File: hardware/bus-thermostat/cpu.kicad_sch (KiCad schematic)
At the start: 28 parts, among them J1 Conn_01x03_Female, J2 RJ45_Shielded, U7 ATtiny424-X, U8 PCA9615DP, U9 MC33660BEFR2

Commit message: Redid the 24VAC path entirely.
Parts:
- renumbered C13 to C21, C14 to C22, C15 to C23, C16 to C24, D11 to D10, D6 to D5, D7 to D6, D8 to D7, D9 to D8, D10 to D9, R20 to R21, R21 to R22, R22 to R23, R23 to R24, R24 to R25, R25 to R26, R26 to R27, R27 to R28, R28 to R29, R29 to R30, R30 to R31, R31 to R32, R32 to R33

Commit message: First rev of thermostat firmware
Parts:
- removed J1: Conn_01x03_Female, symbol Connector:Conn_01x03_Female
- added D?: BAT42W-V, Diode_SMD:D_SOD-123, symbol Diode:BAT42W-V
- added J?: FTDI Serial, SparkFun-Connectors:6_PIN_SERIAL_TARGET_SIDE_W_SILK, symbol SparkFun-Connectors:6_PIN_SERIAL_TARGETSILK
- added JP?: Solder Jumper, Jumper:SolderJumper-2_P1.3mm_Open_TrianglePad1.0x1.5mm, symbol Jumper:SolderJumper_2_Open
- added R?: 470R, symbol Device:R
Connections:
- net +3V3: now also JP?.2 (B)
- net GND: now also J?.GND (6)
- net I2C_EN: no longer U7.7 (PB2)
- net K_LINE_RX: now also U7.6 (PB3); no longer U7.12 (PA2)
- net K_LINE_TX: now also R29.2, U7.7 (PB2); no longer U7.11 (PA1)
- net UPDI: now also D?.2 (A), J?.RXI (2)
- net ~{RESET}: now also U7.12 (PA2); no longer R29.2, U7.6 (PB3)
- new net: D?.1 (K), R?.1
- new net: J?.TXO (3), R?.2
- new net: J?.VCC (4), JP?.1 (A)
- new net OSC_PRIME: U7.11 (PA1)
- no-connect marks 4 -> 6

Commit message: Rework the AC path generation again. Opamps only.
- awaiting the completion of analog circuit analysis
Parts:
- gave numbers to parts that had none: 4
- renumbered D8 to D10, D9 to D11, D10 to D12, D5 to D6, D6 to D7, D7 to D8, J2 to J4, R21 to R23, R22 to R24, R23 to R25, R24 to R26, R25 to R27, R26 to R28, R27 to R29, R28 to R30, R29 to R31, R30 to R32, R31 to R33, R32 to R34, R33 to R36, U9 to U10, U7 to U8, U8 to U9

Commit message: Update some components
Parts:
- removed D10: D, symbol Device:D
- added D10: ACDBQC0130L-HF, Diode_SMD:D_SOD-923, symbol Device:D_Schottky
- D11: value 45V Zener -> MMSZ5260C-E3-08; footprint (none) -> Diode_SMD:D_SOD-123
- D12: value 27V Zener -> BZT52C27-7-F; footprint (none) -> Diode_SMD:D_SOD-123
- D6, D7, D8: footprint (none) -> LED_SMD:LED_0805_2012Metric_Pad1.15x1.40mm_HandSolder
- J4: footprint (none) -> SparkFun-Connectors:RJ45-8
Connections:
- net +12V: now also D10.2 (A)
- net at R36.1: now also D10.1 (K)
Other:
- note added: "27V Zener 500mw"
- note added: "43V Zener 500mW"

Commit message: Fix oscillator, add fan controller/thermostat and its IOs.
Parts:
- added R37: 10k, Resistor_SMD:R_0805_2012Metric_Pad1.20x1.40mm_HandSolder, symbol Device:R
- C23: renamed from C21; footprint (none) -> Capacitor_SMD:C_0805_2012Metric_Pad1.18x1.45mm_HandSolder
- C24: renamed from C22; footprint (none) -> Capacitor_SMD:C_0805_2012Metric_Pad1.18x1.45mm_HandSolder
- C25: renamed from C23; footprint (none) -> Capacitor_SMD:C_0805_2012Metric_Pad1.18x1.45mm_HandSolder
- C26: renamed from C24; footprint (none) -> Capacitor_SMD:C_0805_2012Metric_Pad1.18x1.45mm_HandSolder
- J3: footprint SparkFun-Connectors:6_PIN_SERIAL_TARGET_SIDE_W_SILK -> Beirdo:FTDI_BASIC
- R28: renamed from R23; footprint (none) -> Resistor_SMD:R_0805_2012Metric_Pad1.20x1.40mm_HandSolder
- R29: renamed from R24; footprint (none) -> Resistor_SMD:R_0805_2012Metric_Pad1.20x1.40mm_HandSolder
- R30: renamed from R25; footprint (none) -> Resistor_SMD:R_0805_2012Metric_Pad1.20x1.40mm_HandSolder
- R31: renamed from R26; footprint (none) -> Resistor_SMD:R_0805_2012Metric_Pad1.20x1.40mm_HandSolder
- R32: renamed from R27; footprint (none) -> Resistor_SMD:R_0805_2012Metric_Pad1.20x1.40mm_HandSolder
- R33: renamed from R28; footprint (none) -> Resistor_SMD:R_0805_2012Metric_Pad1.20x1.40mm_HandSolder
- R34: renamed from R29; footprint (none) -> Resistor_SMD:R_0805_2012Metric_Pad1.20x1.40mm_HandSolder
- R35: renamed from R30; footprint (none) -> Resistor_SMD:R_0805_2012Metric_Pad1.20x1.40mm_HandSolder
- R36: renamed from R31; footprint (none) -> Resistor_SMD:R_0805_2012Metric_Pad1.20x1.40mm_HandSolder
- R38: renamed from R32; footprint (none) -> Resistor_SMD:R_0805_2012Metric_Pad1.20x1.40mm_HandSolder
- R39: renamed from R33; footprint (none) -> Resistor_SMD:R_0805_2012Metric_Pad1.20x1.40mm_HandSolder
- R40: renamed from R34; footprint (none) -> Resistor_SMD:R_0805_2012Metric_Pad1.20x1.40mm_HandSolder
- R41: renamed from R35; footprint (none) -> Resistor_SMD:R_0805_2012Metric_Pad1.20x1.40mm_HandSolder
- R42: renamed from R36; footprint (none) -> Resistor_SMD:R_0805_2012Metric_Pad1.20x1.40mm_HandSolder
- renumbered U9 to U10, U10 to U11, U8 to U9
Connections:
- net OSC_PRIME is gone; now on net K_LINE_EN: U9.11 (PA1)
- net +3V3: now also R37.1
- net K_LINE_EN: no longer U9.13 (PA3)
- net ~{K_LINE_LED}: now also U9.13 (PA3); no longer U9.4 (PA6)
- new net ~{FAN_FAULT}: R37.2, U9.4 (PA6)
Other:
- moved on the sheet: C23

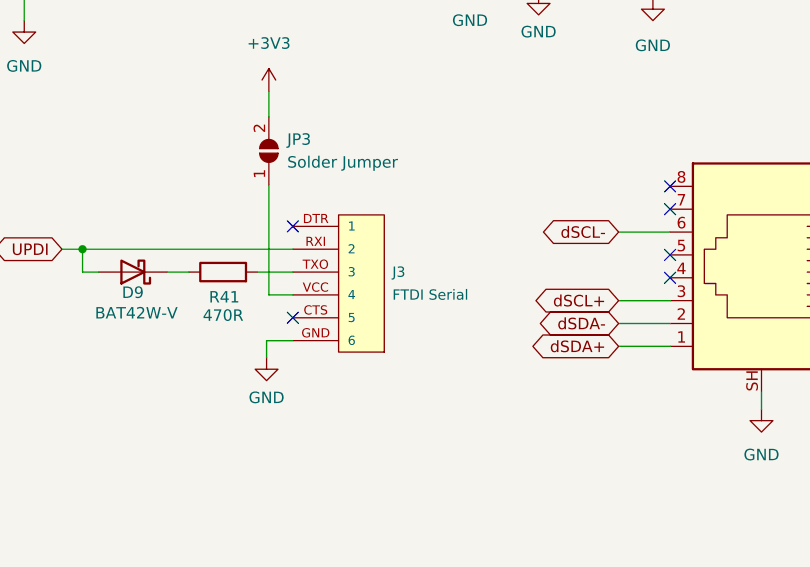
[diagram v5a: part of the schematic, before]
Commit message: Added serial ports
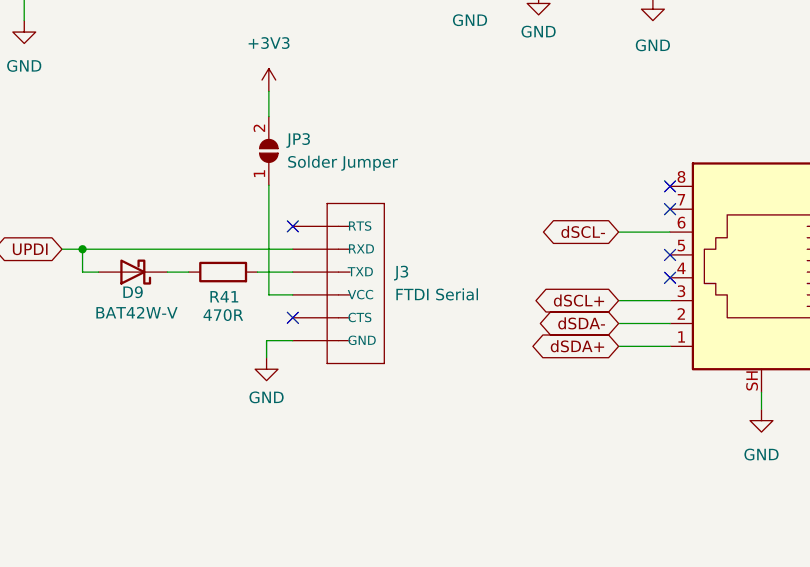
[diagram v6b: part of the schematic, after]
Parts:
- removed J3: FTDI Serial, Beirdo:FTDI_BASIC, symbol SparkFun-Connectors:6_PIN_SERIAL_TARGETSILK
- added J3: FTDI Serial, FTDI_BASIC, symbol Beirdo:FTDI_BASICPTH
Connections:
- net GND: now also J3.1 (GND)
- net UPDI: now also J3.5 (RXD)
- net at R41.2: now also J3.4 (TXD)
- net at JP3.1 (A): now also J3.3 (VCC)
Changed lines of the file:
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@@
     (pin "1")
+  )
+  (symbol (lib_id "Beirdo:FTDI_BASICPTH") (at 212.725 142.24 0) (mirror y) (unit 1)
+    (in_bom yes) (on_board yes) (fields_autoplaced)
+    (property "Reference" "J3" (id 0) (at 218.9734 139.6999 0)
+      (effects (font (size 1.27 1.27)) (justify right))
+    )
+    (property "Value" "FTDI Serial" (id 1) (at 218.9734 142.2399 0)
+      (effects (font (size 1.27 1.27)) (justify right))
+    )
+    (property "Footprint" "FTDI_BASIC" (id 2) (at 211.963 138.43 0)
+      (effects (font (size 0.508 0.508)) hide)
+    )
+    (property "Datasheet" "" (id 3) (at 212.725 142.24 0)
+      (effects (font (size 1.524 1.524)))
+    )
+    (pin "1")
+    (pin "2")
+    (pin "3")
+    (pin "4")
+    (pin "5")
+    (pin "6")
   )
   (symbol (lib_id "Device:R") (at 40.005 122.555 0) (unit 1)
@@
     (pin "1")
   )
-  (symbol (lib_id "SparkFun-Connectors:6_PIN_SERIAL_TARGETSILK") (at 212.725 134.62 180) (unit 1)
-    (in_bom yes) (on_board yes) (fields_autoplaced)
-    (property "Reference" "J3" (id 0) (at 218.694 139.7 0)
-      (effects (font (size 1.143 1.143)) (justify right))
-    )
-    (property "Value" "FTDI Serial" (id 1) (at 218.694 142.24 0)
-      (effects (font (size 1.143 1.143)) (justify right))
-    )
-    (property "Footprint" "Beirdo:FTDI_BASIC" (id 2) (at 212.725 152.4 0)
-      (effects (font (size 0.508 0.508)) hide)
-    )
-    (property "Datasheet" "" (id 3) (at 212.725 134.62 0)
-      (effects (font (size 1.27 1.27)) hide)
-    )
-    (property "Field4" "XXX-00000" (id 4) (at 219.583 137.795 0)
-      (effects (font (size 1.524 1.524)) (justify right) hide)
-    )
-    (pin "CTS")
-    (pin "DTR")
-    (pin "GND")
-    (pin "RXI")
-    (pin "TXO")
-    (pin "VCC")
-  )
   (symbol (lib_id "Device:D_Zener") (at 245.11 60.579 270) (unit 1)

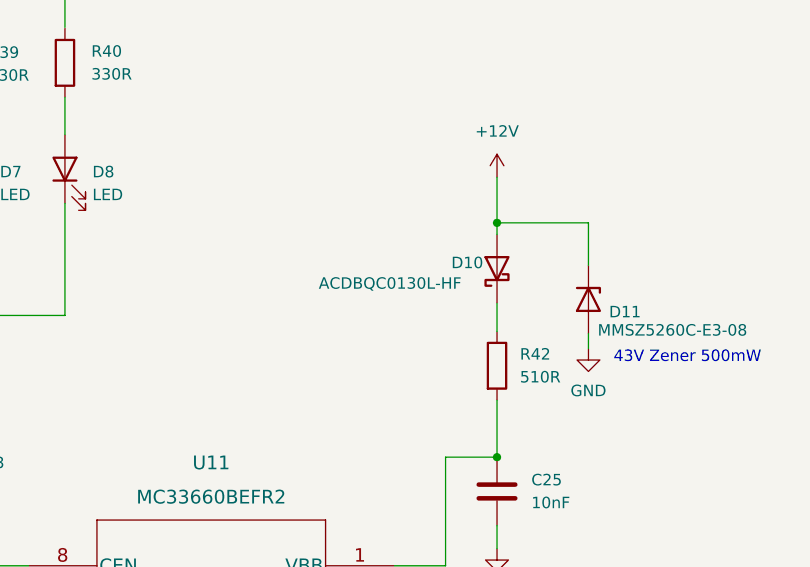
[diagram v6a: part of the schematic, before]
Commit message: Misc changes, move the git libs to new repo
- https://github.com/Beirdo/KiCad-Git-Libraries
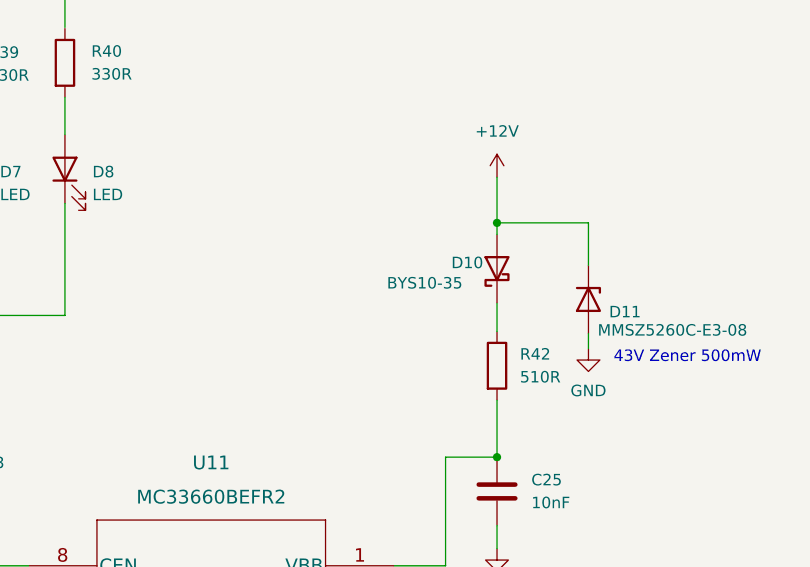
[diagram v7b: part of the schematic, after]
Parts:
- D10: value ACDBQC0130L-HF -> BYS10-35; footprint Diode_SMD:D_SOD-923 -> Diode_SMD:D_SMA_Handsoldering
- J3: footprint FTDI_BASIC -> Beirdo:FTDI_BASIC

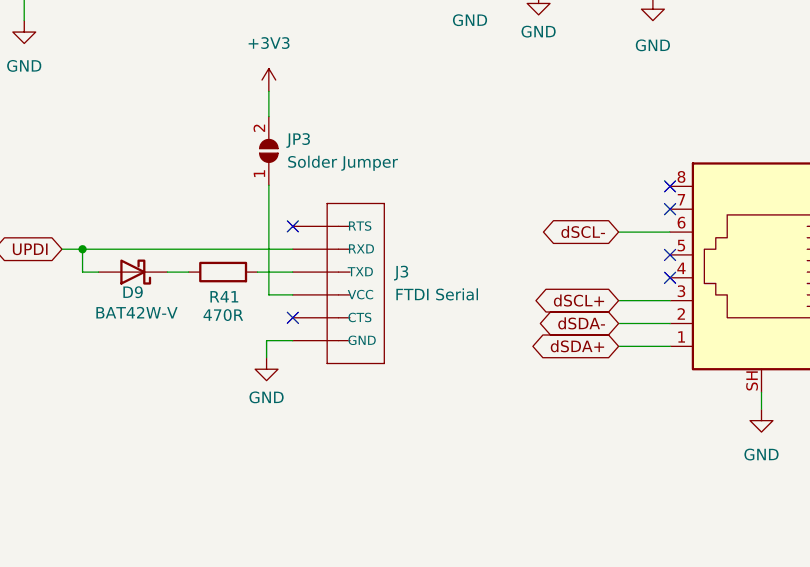
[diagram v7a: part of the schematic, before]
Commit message: Moved over to PlatformIO
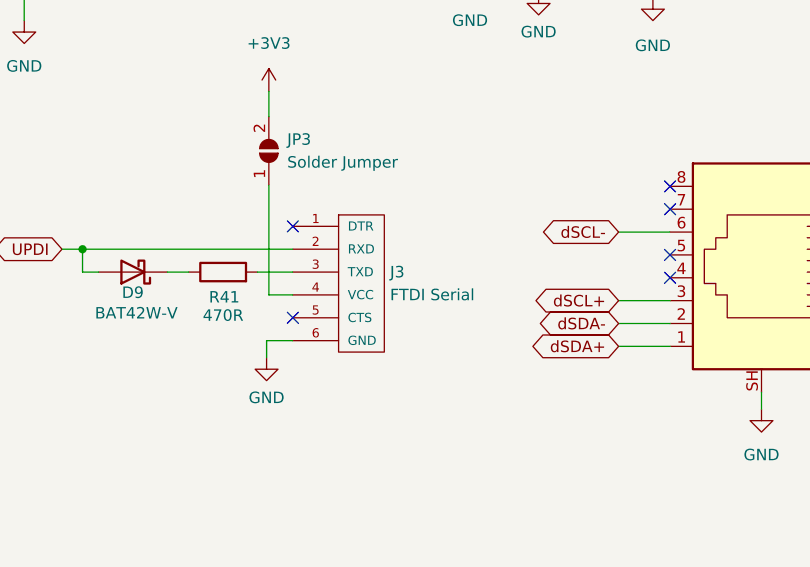
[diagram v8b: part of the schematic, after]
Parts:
- J3: footprint Beirdo:FTDI_BASIC -> Beirdo:FTDI-TARGET; symbol Beirdo:FTDI_BASICPTH -> Beirdo:FTDI-TARGET
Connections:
- net GND: now also J3.6 (GND); no longer J3.1 (GND)
- net UPDI: now also J3.2 (RXD); no longer J3.5 (RXD)
- net at R41.2: now also J3.3 (TXD); no longer J3.4 (TXD)
- net at JP3.1 (A): now also J3.4 (VCC); no longer J3.3 (VCC)
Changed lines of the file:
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@@
     (pin "1")
   )
-  (symbol (lib_id "Beirdo:FTDI_BASICPTH") (at 212.725 142.24 0) (mirror y) (unit 1)
+  (symbol (lib_id "Beirdo:FTDI-TARGET") (at 215.265 133.35 0) (unit 1)
     (in_bom yes) (on_board yes) (fields_autoplaced)
-    (property "Reference" "J3" (id 0) (at 218.9734 139.6999 0)
-      (effects (font (size 1.27 1.27)) (justify right))
+    (property "Reference" "J3" (id 0) (at 218.44 139.6999 0)
+      (effects (font (size 1.27 1.27)) (justify left))
     )
-    (property "Value" "FTDI Serial" (id 1) (at 218.9734 142.2399 0)
-      (effects (font (size 1.27 1.27)) (justify right))
+    (property "Value" "FTDI Serial" (id 1) (at 218.44 142.2399 0)
+      (effects (font (size 1.27 1.27)) (justify left))
     )
-    (property "Footprint" "Beirdo:FTDI_BASIC" (id 2) (at 211.963 138.43 0)
+    (property "Footprint" "Beirdo:FTDI-TARGET" (id 2) (at 215.265 152.4 0)
       (effects (font (size 0.508 0.508)) hide)
     )
